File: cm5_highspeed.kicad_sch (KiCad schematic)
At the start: 1 part

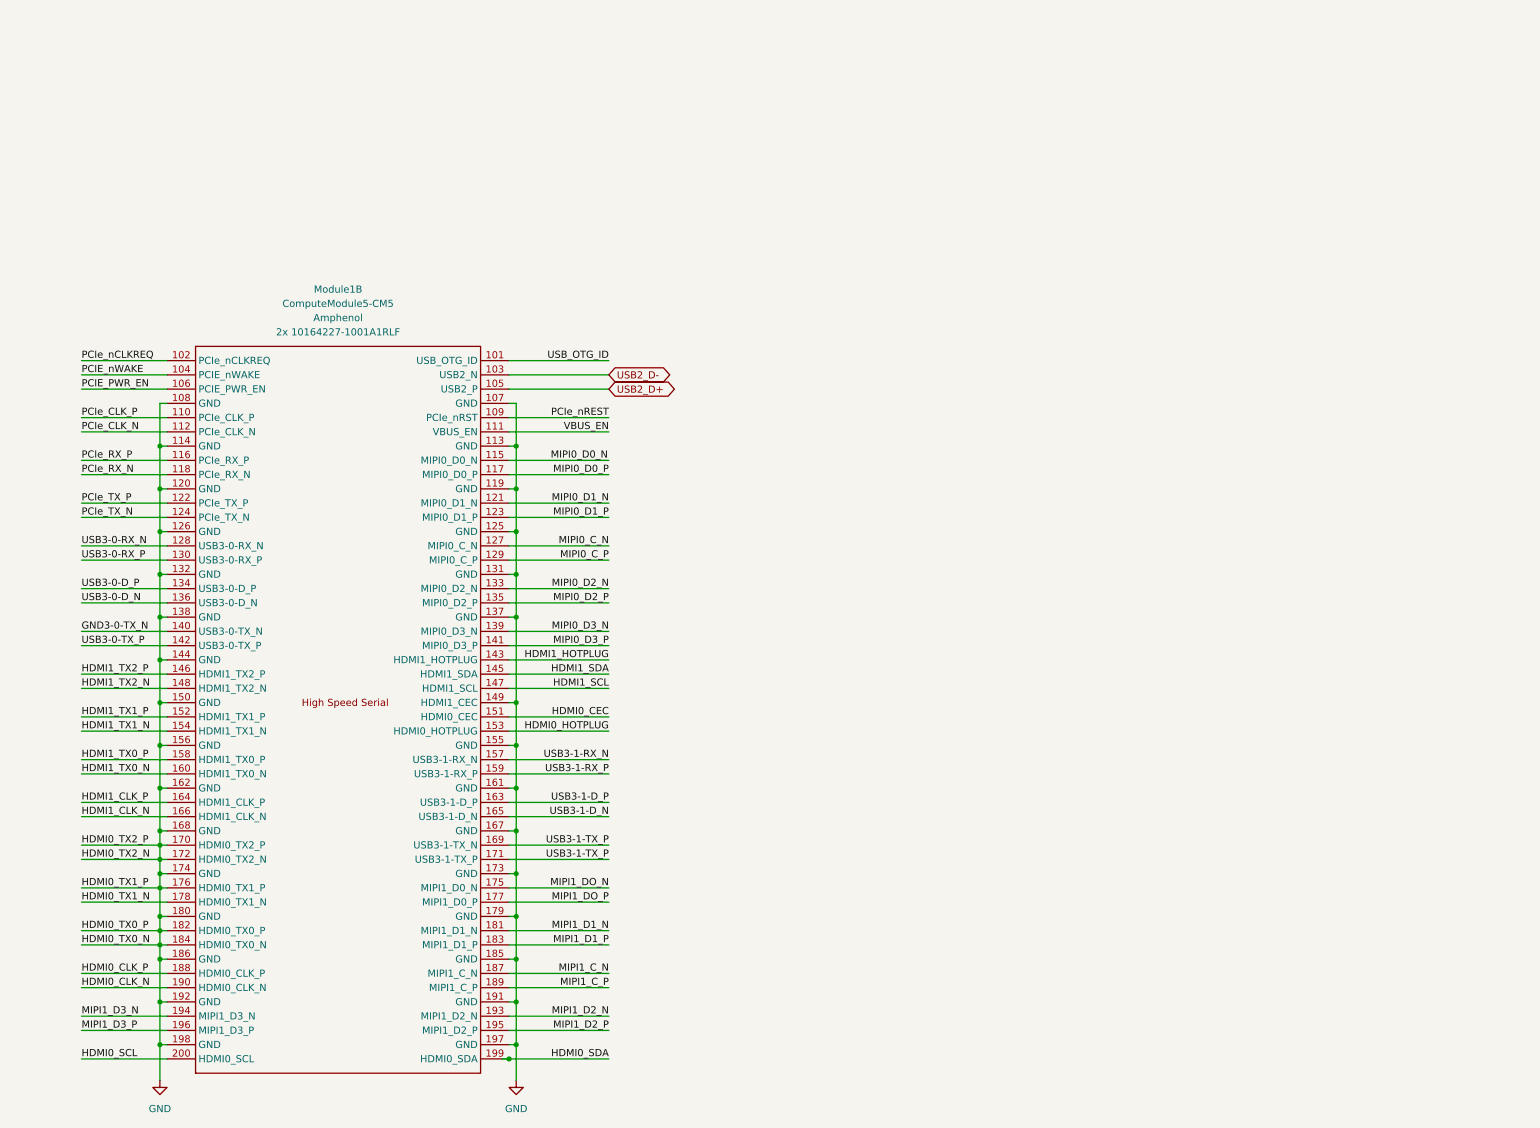
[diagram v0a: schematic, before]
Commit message: create high-speed connects sheet
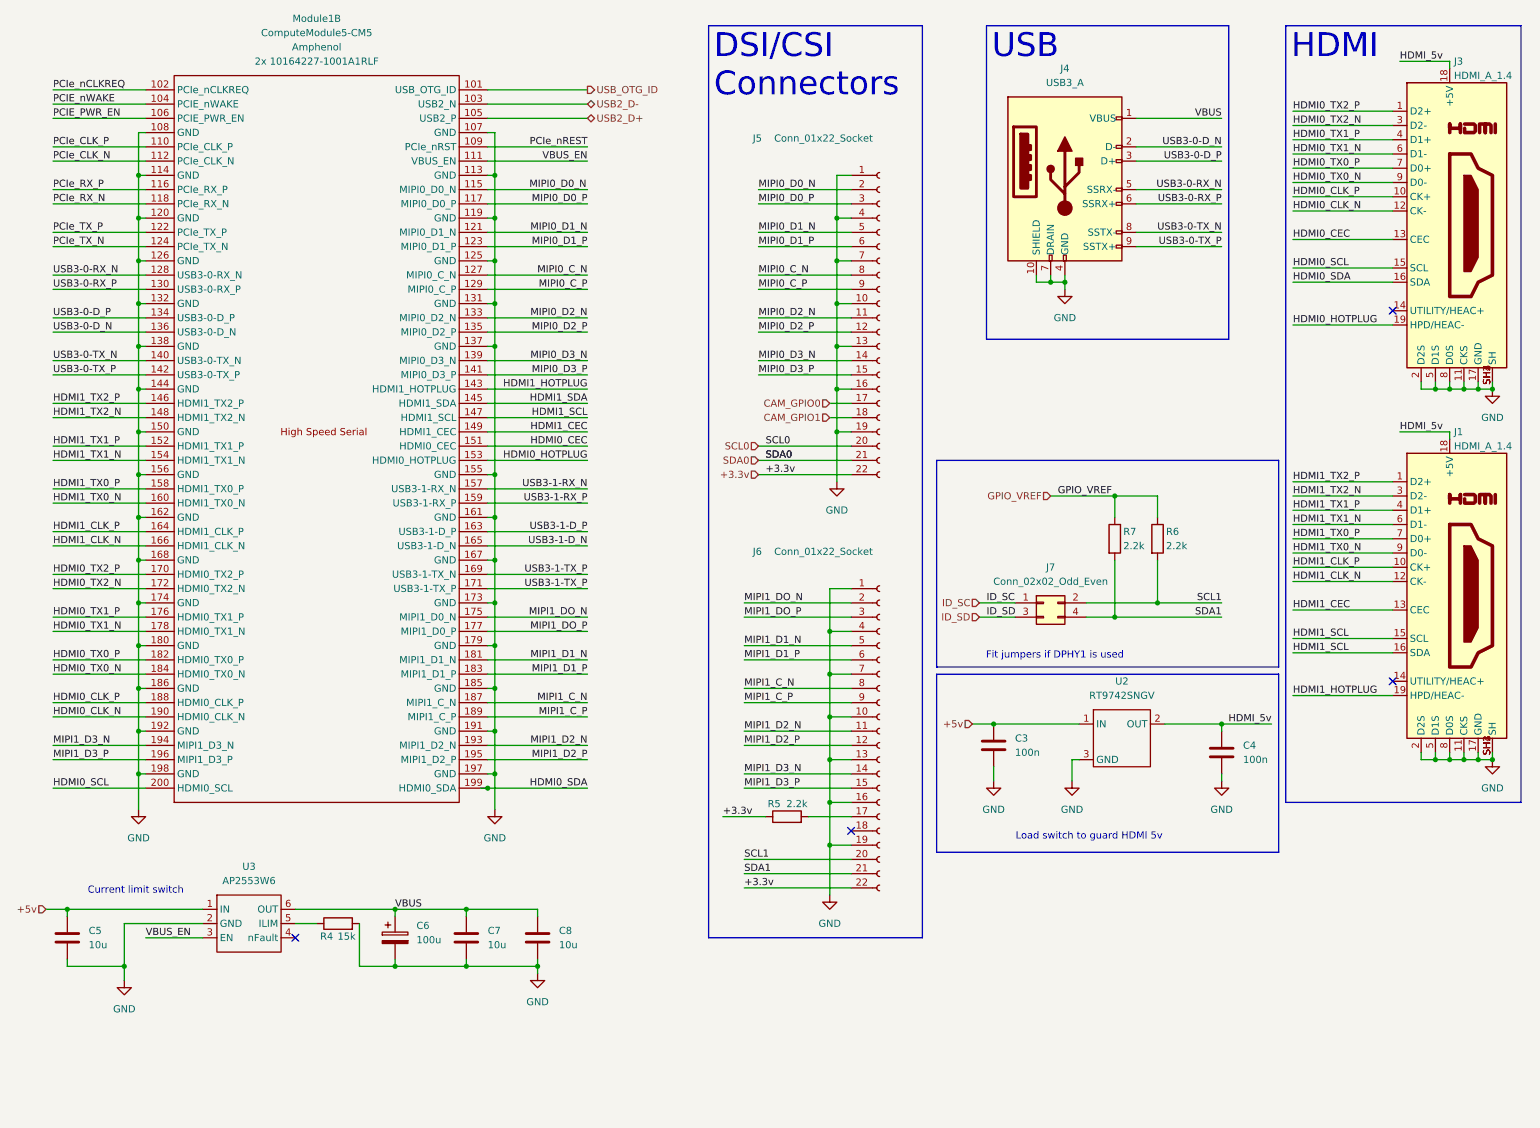
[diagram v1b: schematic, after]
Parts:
- added C3, C4: 100n, symbol Device:C
- added C5, C7, C8: 10u, symbol Device:C
- added C6: 100u, symbol Device:C_Polarized
- added J1, J3: HDMI_A_1.4, symbol CM5IO:HDMI_A_1.4
- added J4: USB3_A, symbol Connector:USB3_A
- added J5, J6: Conn_01x22_Socket, symbol Connector:Conn_01x22_Socket
- added J7: Conn_02x02_Odd_Even, symbol Connector_Generic:Conn_02x02_Odd_Even
- added R4: 15k, symbol Device:R
- added R5, R6, R7: 2.2k, symbol Device:R
- added U2: RT9742SNGV, Package_TO_SOT_SMD:TSOT-23_HandSoldering, symbol CM5IO:RT9742SNGV
- added U3: AP2553W6, Package_TO_SOT_SMD:SOT-23-6, symbol CM5IO:AP2553W6
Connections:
- net GND: now also C3.2, C4.2, C5.2, C6.2, C7.2, C8.2, J1.11 (CKS), J1.17 (GND), J1.2 (D2S), J1.5 (D1S), J1.8 (D0S), J1.SH1 (SH), J1.SH2 (SH), J1.SH3 (SH), J1.SH4 (SH), J3.11 (CKS), J3.17 (GND), J3.2 (D2S), J3.5 (D1S), J3.8 (D0S), J3.SH1 (SH), J3.SH2 (SH), J3.SH3 (SH), J3.SH4 (SH), J4.10 (SHIELD), J4.4 (GND), J4.7 (DRAIN), J5.1 (Pin_1), J5.10 (Pin_10), J5.13 (Pin_13), J5.16 (Pin_16), J5.19 (Pin_19), J5.4 (Pin_4), J5.7 (Pin_7), J6.1 (Pin_1), J6.10 (Pin_10), J6.13 (Pin_13), J6.16 (Pin_16), J6.19 (Pin_19), J6.4 (Pin_4), J6.7 (Pin_7), R4.2, U2.3 (GND), U3.2 (GND); no longer Module1.149 (HDMI1_CEC), Module1.170 (HDMI0_TX2_P), Module1.172 (HDMI0_TX2_N), Module1.176 (HDMI0_TX1_P), Module1.182 (HDMI0_TX0_P), Module1.184 (HDMI0_TX0_N)
- net HDMI0_CEC: now also J3.13 (CEC)
- net HDMI0_CLK_N: now also J3.12 (CK-)
- net HDMI0_CLK_P: now also J3.10 (CK+)
- net HDMI0_HOTPLUG: now also J3.19 (HPD/HEAC-)
- net HDMI0_SCL: now also J3.15 (SCL)
- net HDMI0_SDA: now also J3.16 (SDA)
- net HDMI0_TX1_N: now also J3.6 (D1-)
- net HDMI1_CLK_N: now also J1.12 (CK-)
- net HDMI1_CLK_P: now also J1.10 (CK+)
- net HDMI1_HOTPLUG: now also J1.19 (HPD/HEAC-)
- net HDMI1_SCL: now also J1.15 (SCL), J1.16 (SDA)
- net HDMI1_TX0_N: now also J1.9 (D0-)
- net HDMI1_TX0_P: now also J1.7 (D0+)
- net HDMI1_TX1_N: now also J1.6 (D1-)
- net HDMI1_TX1_P: now also J1.4 (D1+)
- net HDMI1_TX2_N: now also J1.3 (D2-)
- net HDMI1_TX2_P: now also J1.1 (D2+)
- net MIPI0_C_N: now also J5.8 (Pin_8)
- net MIPI0_C_P: now also J5.9 (Pin_9)
- net MIPI0_D0_N: now also J5.2 (Pin_2)
- net MIPI0_D0_P: now also J5.3 (Pin_3)
- net MIPI0_D1_N: now also J5.5 (Pin_5)
- net MIPI0_D1_P: now also J5.6 (Pin_6)
- net MIPI0_D2_N: now also J5.11 (Pin_11)
- net MIPI0_D2_P: now also J5.12 (Pin_12)
- net MIPI0_D3_N: now also J5.14 (Pin_14)
- net MIPI0_D3_P: now also J5.15 (Pin_15)
- net MIPI1_C_N: now also J6.8 (Pin_8)
- net MIPI1_C_P: now also J6.9 (Pin_9)
- net MIPI1_D1_N: now also J6.5 (Pin_5)
- net MIPI1_D1_P: now also J6.6 (Pin_6)
- net MIPI1_D2_N: now also J6.11 (Pin_11)
- net MIPI1_D2_P: now also J6.12 (Pin_12)
- net MIPI1_D3_N: now also J6.14 (Pin_14)
- net MIPI1_D3_P: now also J6.15 (Pin_15)
- net MIPI1_DO_N: now also J6.2 (Pin_2)
- net MIPI1_DO_P: now also J6.3 (Pin_3)
- net USB3-0-D_N: now also J4.2 (D-)
- net USB3-0-D_P: now also J4.3 (D+)
- net USB3-0-RX_N: now also J4.5 (SSRX-)
- net USB3-0-RX_P: now also J4.6 (SSRX+)
- net USB3-0-TX_P: now also J4.9 (SSTX+)
- net VBUS_EN: now also U3.3 (EN)
- net GND3-0-TX_N renamed USB3-0-TX_N
- net USB3-0-TX_N: now also J4.8 (SSTX-)
- new net: J6.17 (Pin_17), R5.2
- new net: R4.1, U3.5 (ILIM)
- new net +3.3v: J5.22 (Pin_22), J6.22 (Pin_22), R5.1
- new net +5v: C3.1, C5.1, U2.1 (IN), U3.1 (IN)
- new net CAM_GPIO0: J5.17 (Pin_17)
- new net CAM_GPIO1: J5.18 (Pin_18)
- new net GPIO_VREF: R6.1, R7.1
- new net HDMI0_TX0_N: J3.9 (D0-), Module1.184 (HDMI0_TX0_N)
- new net HDMI0_TX0_P: J3.7 (D0+), Module1.182 (HDMI0_TX0_P)
- new net HDMI0_TX1_P: J3.4 (D1+), Module1.176 (HDMI0_TX1_P)
- new net HDMI0_TX2_N: J3.3 (D2-), Module1.172 (HDMI0_TX2_N)
- new net HDMI0_TX2_P: J3.1 (D2+), Module1.170 (HDMI0_TX2_P)
- new net HDMI1_CEC: J1.13 (CEC), Module1.149 (HDMI1_CEC)
- new net HDMI_5v: C4.1, J1.18 (+5V), J3.18 (+5V), U2.2 (OUT)
- new net ID_SC: J7.1 (Pin_1)
- new net ID_SD: J7.3 (Pin_3)
- new net SCL0: J5.20 (Pin_20)
- new net SCL1: J6.20 (Pin_20), J7.2 (Pin_2), R6.2
- new net SDA0: J5.21 (Pin_21)
- new net SDA1: J6.21 (Pin_21), J7.4 (Pin_4), R7.2
- new net VBUS: C6.1, C7.1, C8.1, J4.1 (VBUS), U3.6 (OUT)
- no-connect marks 0 -> 4
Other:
- note added: "Current limit switch"
- note added: "Fit jumpers if DPHY1 is used"
- note added: "Load switch to guard HDMI 5v"
- moved on the sheet: Module1B
